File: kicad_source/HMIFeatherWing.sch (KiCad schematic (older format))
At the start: 27 parts, among them CN1 ADAFRUIT_FEATHER, Q1 2N7002, SW1 ALPS_SKRH, SW2 SW_PUSH

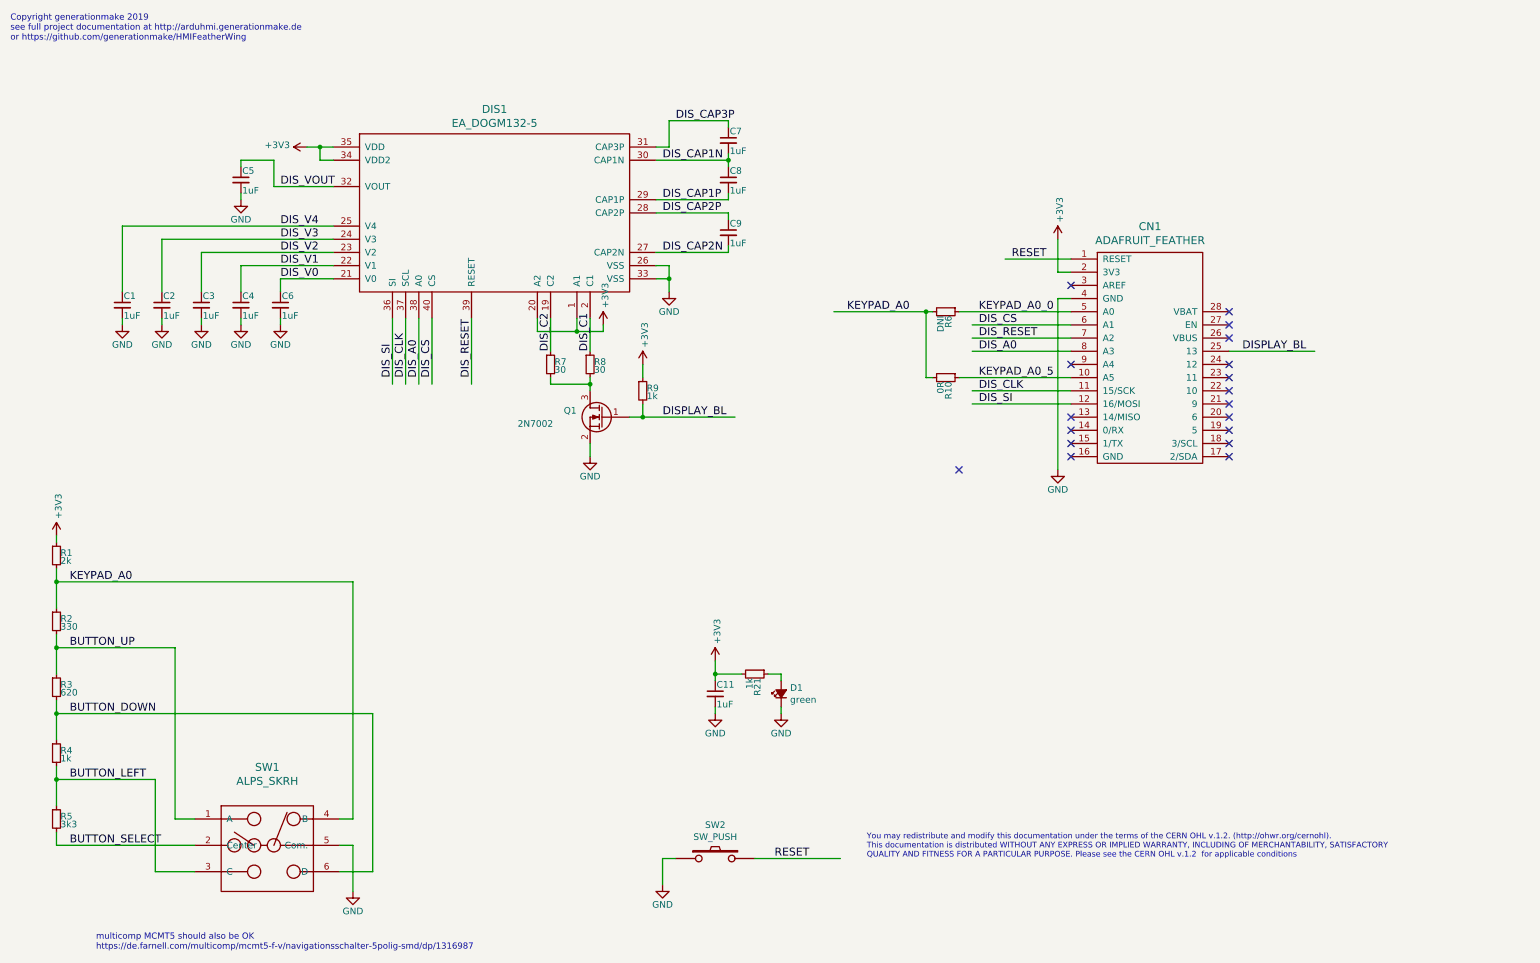
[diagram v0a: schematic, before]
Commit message: started development for 1.1, made pads for ALPS SKRH a little bit longer
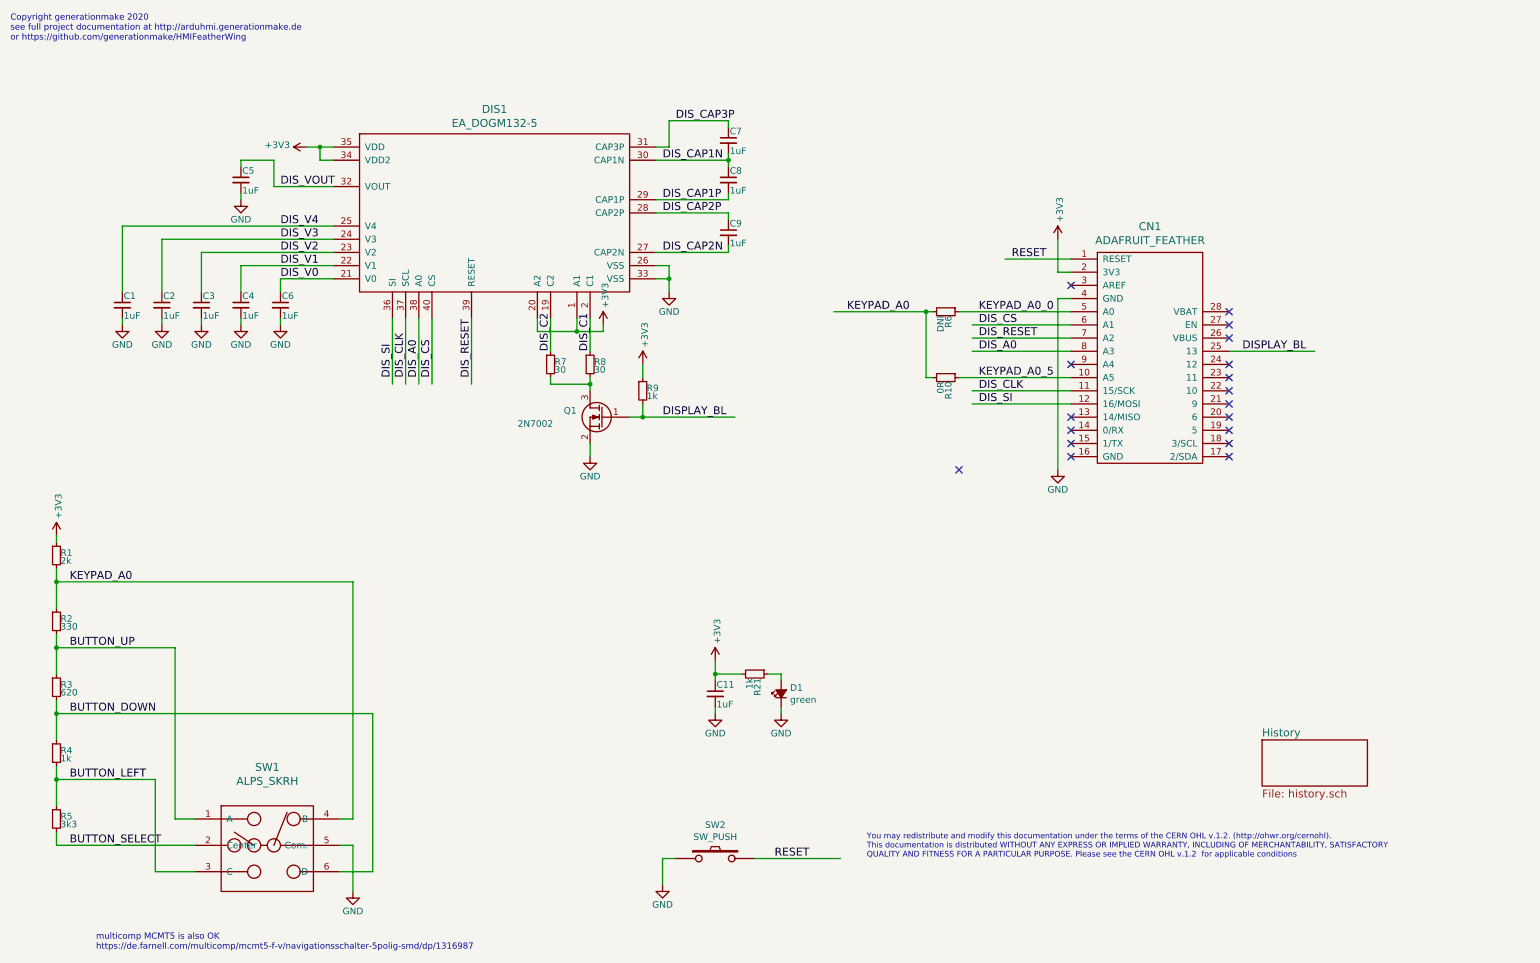
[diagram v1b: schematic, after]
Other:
- note added: "Copyright generationmake 2020\nsee full project documentation at http://arduhmi.generationmake.de\nor https://github.com/generationmake/HMIFeatherWing"
- note added: "multicomp MCMT5 is also OK\nhttps://de.farnell.com/multicomp/mcmt5-f-v/navigationsschalter-5polig-smd/dp/1316987"
- note removed: "Copyright generationmake 2019\nsee full project documentation at http://arduhmi.generationmake.de\nor https://github.com/generationmake/HMIFeatherWing"
- note removed: "multicomp MCMT5 should also be OK\nhttps://de.farnell.com/multicomp/mcmt5-f-v/navigationsschalter-5polig-smd/dp/1316987"
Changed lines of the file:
@@
 $Descr A4 11693 8268
 encoding utf-8
-Sheet 1 1
+Sheet 1 2
 Title "HMIFeatherWing"
-Date "2019-12-27"
-Rev "1.0"
+Date "2020-01-24"
+Rev "1.1"
 Comp "generationmake"
 Comment1 ""
@@
 $EndDescr
 Text Notes 500  700  0    47   ~ 0
-Copyright generationmake 2019\nsee full project documentation at http://arduhmi.generationmake.de\nor https://github.com/generationmake/HMIFeatherWing
+Copyright generationmake 2020\nsee full project documentation at http://arduhmi.generationmake.de\nor https://github.com/generationmake/HMIFeatherWing
 $Comp
 L HMIFeatherWing-rescue:C_0603-ArduHMIShield-rescue-ArduHMIShield-rescue-MKRHMIShield-rescue-MKRHMIShield-rescue C7
@@
 	3100 6800 3100 7150
 Text Notes 1150 7600 0    47   ~ 0
-multicomp MCMT5 should also be OK\nhttps://de.farnell.com/multicomp/mcmt5-f-v/navigationsschalter-5polig-smd/dp/1316987
+multicomp MCMT5 is also OK\nhttps://de.farnell.com/multicomp/mcmt5-f-v/navigationsschalter-5polig-smd/dp/1316987
 $Comp
 L MODULE_compute:ADAFRUIT_FEATHER CN1
@@
 	1    0    0    -1
 $EndComp
+$Sheet
+S 10000 6000 800  350
+U 5E2B29FC
+F0 "History" 60
+F1 "history.sch" 60
+$EndSheet
 $EndSCHEMATC
